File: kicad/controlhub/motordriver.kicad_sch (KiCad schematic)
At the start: 4 parts

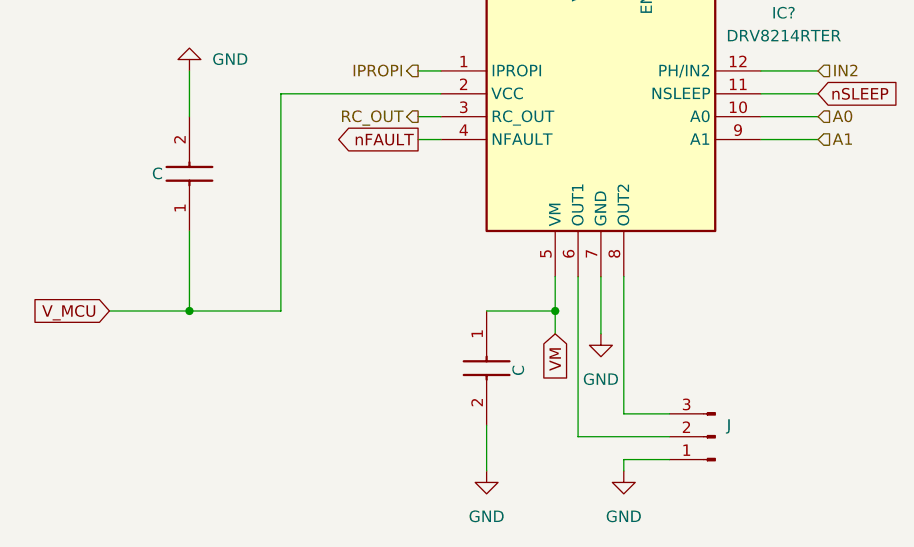
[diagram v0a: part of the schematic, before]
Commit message: fixed small overlap in diagrams
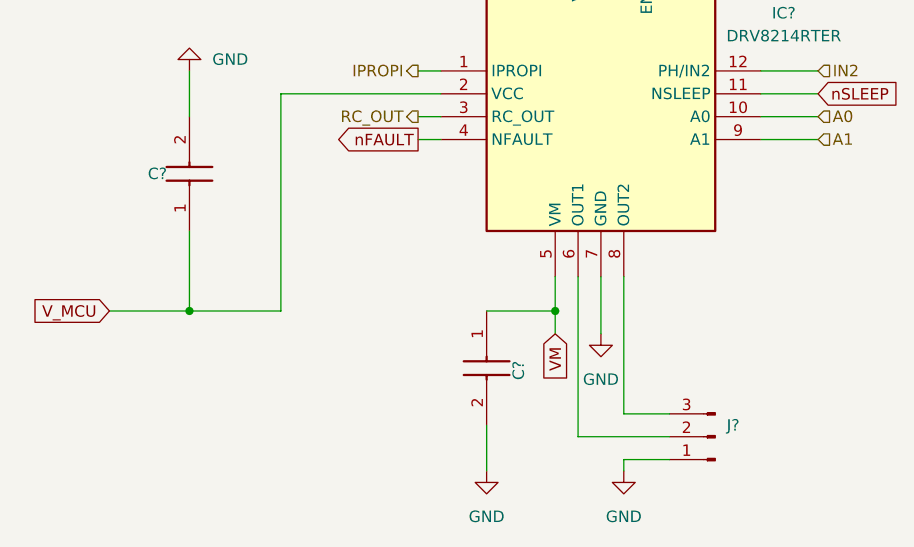
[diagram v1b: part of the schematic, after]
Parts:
- renumbered C to C?, J to J?
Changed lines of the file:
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@@
 		(dnp no)
 		(fields_autoplaced yes)
-		(property "Reference" "#PWR"
+		(property "Reference" "#PWR?"
 			(at 114.3 113.03 0)
 			(effects
@@
 		(instances
 			(project "controlhub"
+				(path "/78f9b8b9-94ed-46bb-ab2b-797c156bf665/5fdbac9f-f658-4a00-a70d-cfad4fe5961e"
+					(reference "#PWR?")
+					(unit 1)
+				)
 				(path "/78f9b8b9-94ed-46bb-ab2b-797c156bf665/69943119-d6be-40ce-897b-194a2d80c196"
 					(reference "#PWR032")
@@
 		(dnp no)
 		(fields_autoplaced yes)
-		(property "Reference" "#PWR"
+		(property "Reference" "#PWR?"
 			(at 81.28 55.88 0)
 			(effects
@@
 		(instances
 			(project "controlhub"
+				(path "/78f9b8b9-94ed-46bb-ab2b-797c156bf665/5fdbac9f-f658-4a00-a70d-cfad4fe5961e"
+					(reference "#PWR?")
+					(unit 1)
+				)
 				(path "/78f9b8b9-94ed-46bb-ab2b-797c156bf665/69943119-d6be-40ce-897b-194a2d80c196"
 					(reference "#PWR031")
@@
 		(dnp no)
 		(fields_autoplaced yes)
-		(property "Reference" "#PWR"
+		(property "Reference" "#PWR?"
 			(at 127 97.79 0)
 			(effects
@@
 		(instances
 			(project "controlhub"
+				(path "/78f9b8b9-94ed-46bb-ab2b-797c156bf665/5fdbac9f-f658-4a00-a70d-cfad4fe5961e"
+					(reference "#PWR?")
+					(unit 1)
+				)
 				(path "/78f9b8b9-94ed-46bb-ab2b-797c156bf665/69943119-d6be-40ce-897b-194a2d80c196"
 					(reference "#PWR039")
@@
 		(dnp no)
 		(fields_autoplaced yes)
-		(property "Reference" "#PWR"
+		(property "Reference" "#PWR?"
 			(at 129.54 113.03 0)
 			(effects
@@
 		(instances
 			(project "controlhub"
+				(path "/78f9b8b9-94ed-46bb-ab2b-797c156bf665/5fdbac9f-f658-4a00-a70d-cfad4fe5961e"
+					(reference "#PWR?")
+					(unit 1)
+				)
 				(path "/78f9b8b9-94ed-46bb-ab2b-797c156bf665/69943119-d6be-40ce-897b-194a2d80c196"
 					(reference "#PWR040")
@@
 		(dnp no)
 		(fields_autoplaced yes)
-		(property "Reference" "#PWR"
+		(property "Reference" "#PWR?"
 			(at 124.46 41.91 0)
 			(effects
@@
 		(instances
 			(project "controlhub"
+				(path "/78f9b8b9-94ed-46bb-ab2b-797c156bf665/5fdbac9f-f658-4a00-a70d-cfad4fe5961e"
+					(reference "#PWR?")
+					(unit 1)
+				)
 				(path "/78f9b8b9-94ed-46bb-ab2b-797c156bf665/69943119-d6be-40ce-897b-194a2d80c196"
 					(reference "#PWR033")
@@
 		(dnp no)
 		(fields_autoplaced yes)
-		(property "Reference" "J"
+		(property "Reference" "J?"
 			(at 140.97 101.5999 0)
 			(effects
@@
 		(instances
 			(project "controlhub"
+				(path "/78f9b8b9-94ed-46bb-ab2b-797c156bf665/5fdbac9f-f658-4a00-a70d-cfad4fe5961e"
+					(reference "J?")
+					(unit 1)
+				)
 				(path "/78f9b8b9-94ed-46bb-ab2b-797c156bf665/69943119-d6be-40ce-897b-194a2d80c196"
 					(reference "J6")
@@
 		(on_board yes)
 		(dnp no)
-		(property "Reference" "C"
+		(property "Reference" "C?"
 			(at 117.856 95.504 0)
 			(effects
@@
 		(instances
 			(project "controlhub"
+				(path "/78f9b8b9-94ed-46bb-ab2b-797c156bf665/5fdbac9f-f658-4a00-a70d-cfad4fe5961e"
+					(reference "C?")
+					(unit 1)
+				)
 				(path "/78f9b8b9-94ed-46bb-ab2b-797c156bf665/69943119-d6be-40ce-897b-194a2d80c196"
 					(reference "C8")
@@
 		(on_board yes)
 		(dnp no)
-		(property "Reference" "C"
+		(property "Reference" "C?"
 			(at 77.724 73.66 90)
 			(effects
@@
 		(instances
 			(project "controlhub"
+				(path "/78f9b8b9-94ed-46bb-ab2b-797c156bf665/5fdbac9f-f658-4a00-a70d-cfad4fe5961e"
+					(reference "C?")
+					(unit 1)
+				)
 				(path "/78f9b8b9-94ed-46bb-ab2b-797c156bf665/69943119-d6be-40ce-897b-194a2d80c196"
 					(reference "C7")
@@
 		)
 	)
-	(sheet_instances
-		(path "/"
-			(page "1")
-		)
-	)
-	(embedded_fonts no)
 )

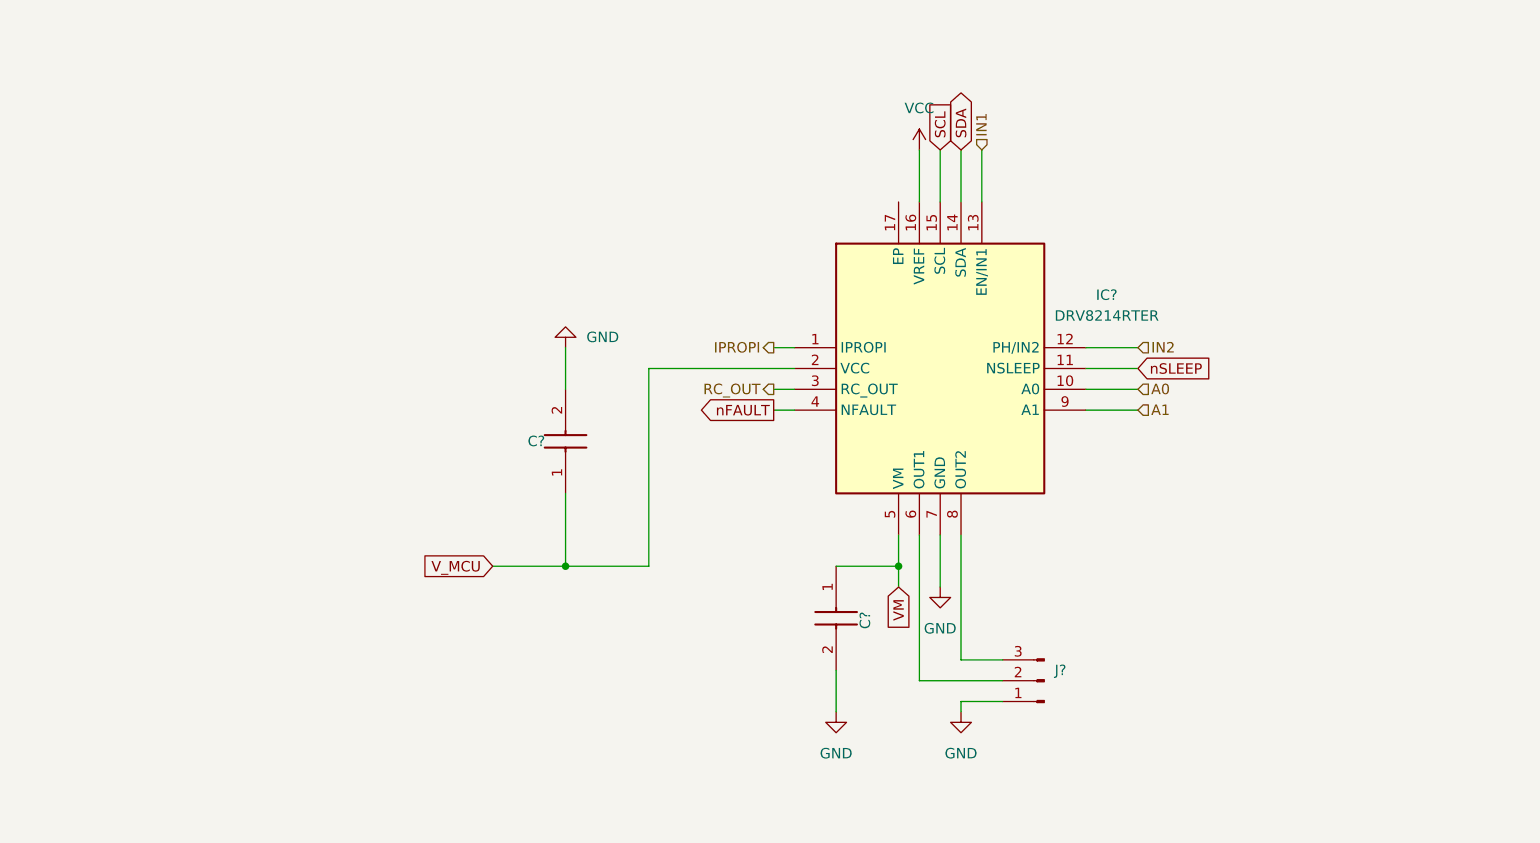
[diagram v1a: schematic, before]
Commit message: removed uneccesary schematics and worked on proper wiring
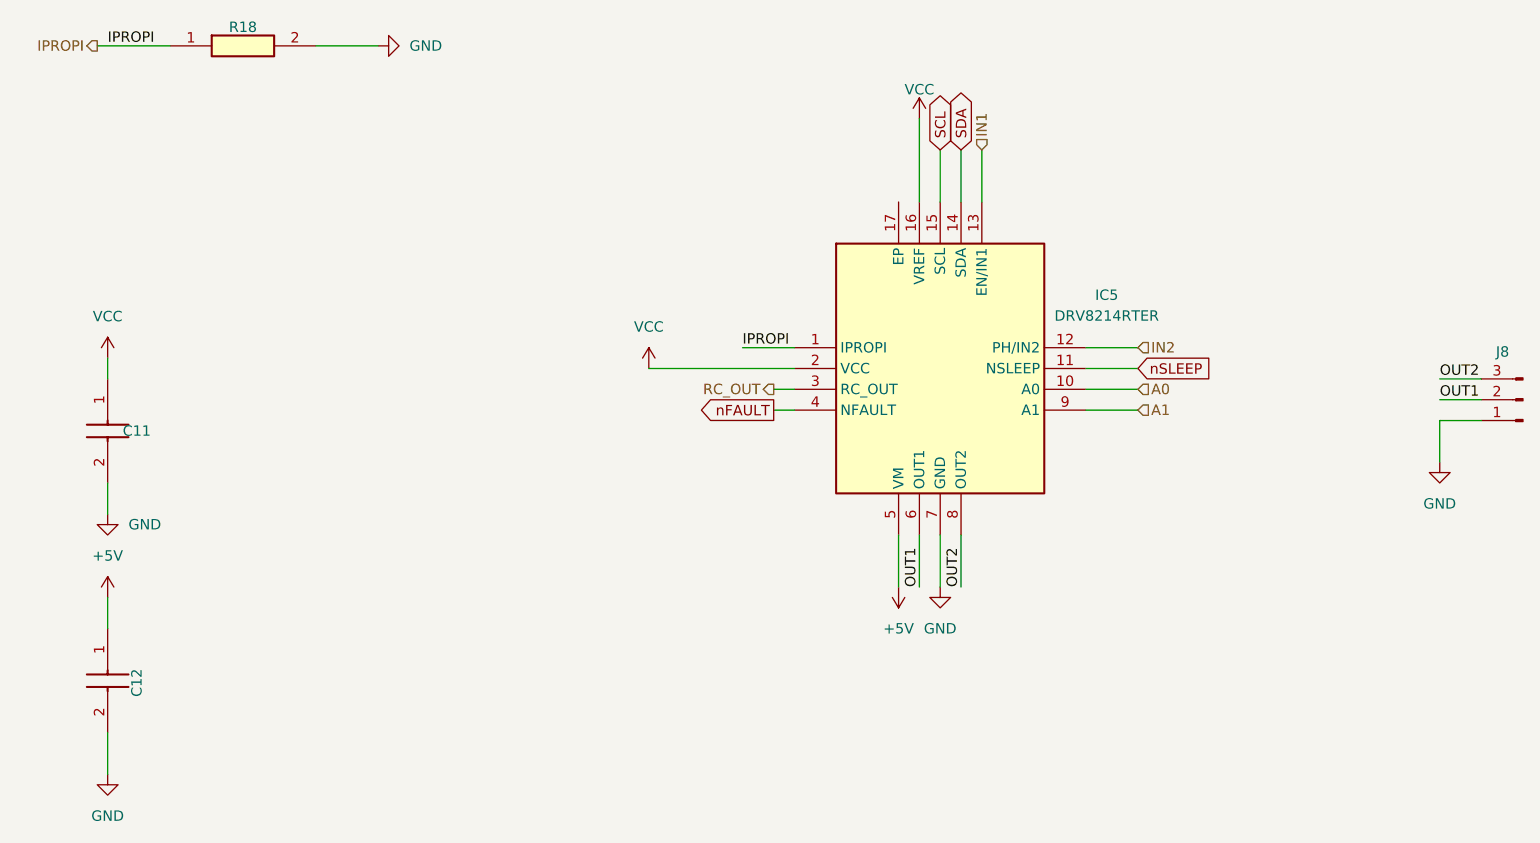
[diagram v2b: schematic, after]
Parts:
- added R18: RC0402FR-075K1L, Resistors:RESC1005X40N, symbol Resistors:RC0402FR-075K1L
- gave numbers to parts that had none: 4
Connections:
- net V_MCU is gone; now on net VCC: C11.1, IC5.2 (VCC)
- net GND: now also R18.2
- net IPROPI: now also R18.1
- net OUT1: now reaches IC5.6 (OUT1), J8.2 (Pin_2)
- net OUT2: now reaches IC5.8 (OUT2), J8.3 (Pin_3)
- net VM renamed +5V
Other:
- moved on the sheet: C11, C12, J8

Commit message: added filters and kept working on wiring schematics
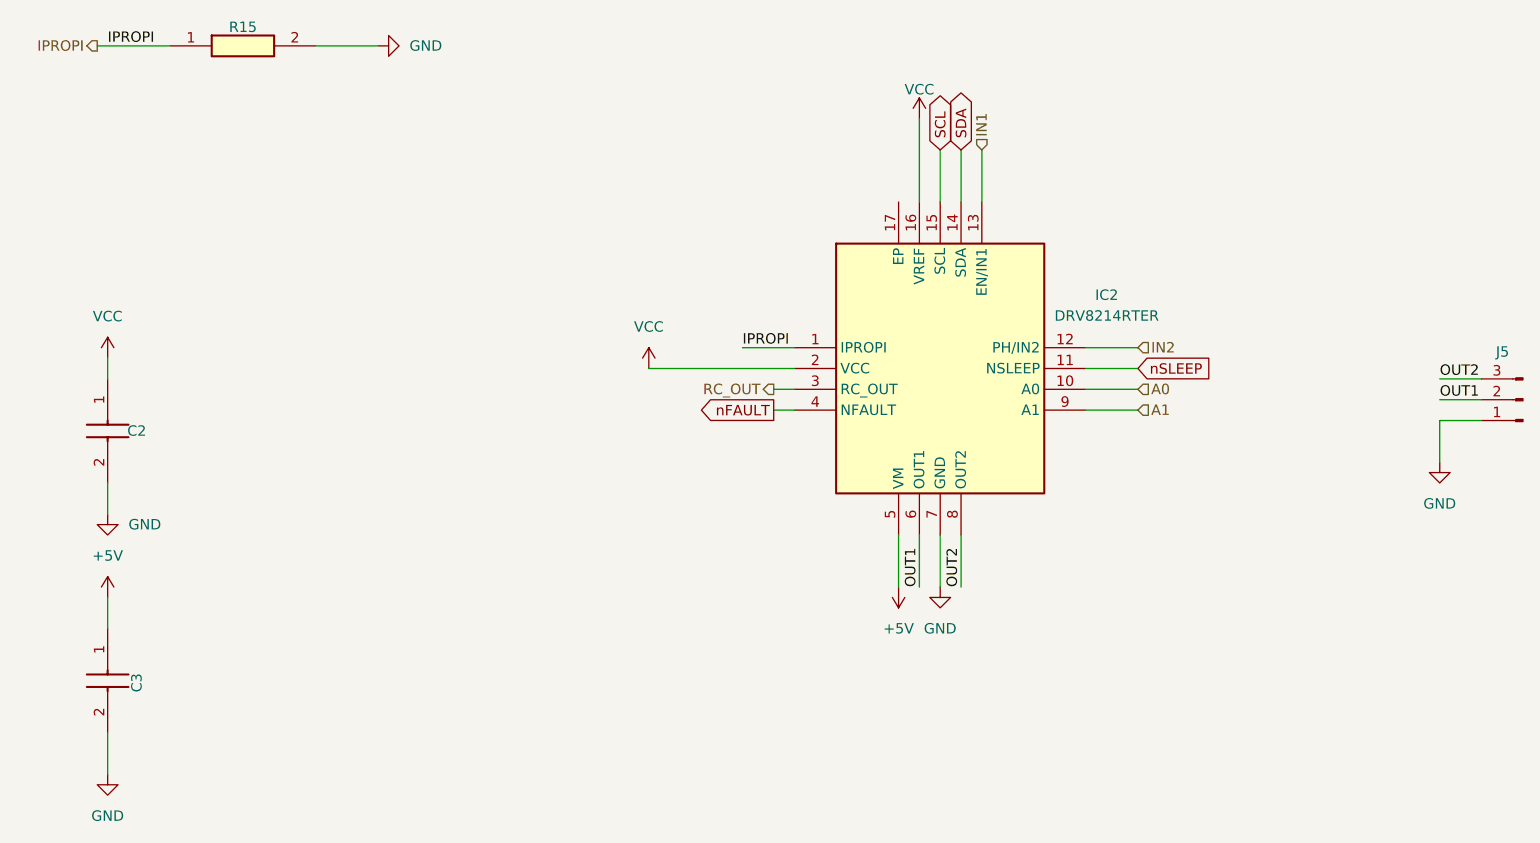
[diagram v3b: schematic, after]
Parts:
- renumbered C11 to C2, C12 to C3, IC5 to IC2, J8 to J5, R18 to R15
